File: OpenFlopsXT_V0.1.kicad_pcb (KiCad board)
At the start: 2 copper layers, 83.9 x 68.6 mm, 77 parts, among them J1 UP, J2 DN, J3 R, J4 G, J5 Conn_01x22_Female, J6 OSHW_LOGO, P1 FLOPPY_CONN, P2 POWER_INPUT, P3 POWER_PASSTHRU, P4 PROG_PORT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

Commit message: Corrected Github URL
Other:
- board text added: "https://github.com/pinnet/OpenFlops"
- board text removed: "https://github.com/pinnet/openflops"
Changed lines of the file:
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@@
     (effects (font (size 0.5 0.5) (thickness 0.125)))
   )
-  (gr_text "https://github.com/pinnet/openflops" (at 124.95 128.005) (layer "F.SilkS")
+  (gr_text "https://github.com/pinnet/OpenFlops" (at 124.95 128.005) (layer "F.SilkS")
     (effects (font (size 0.5 0.5) (thickness 0.125)))
   )

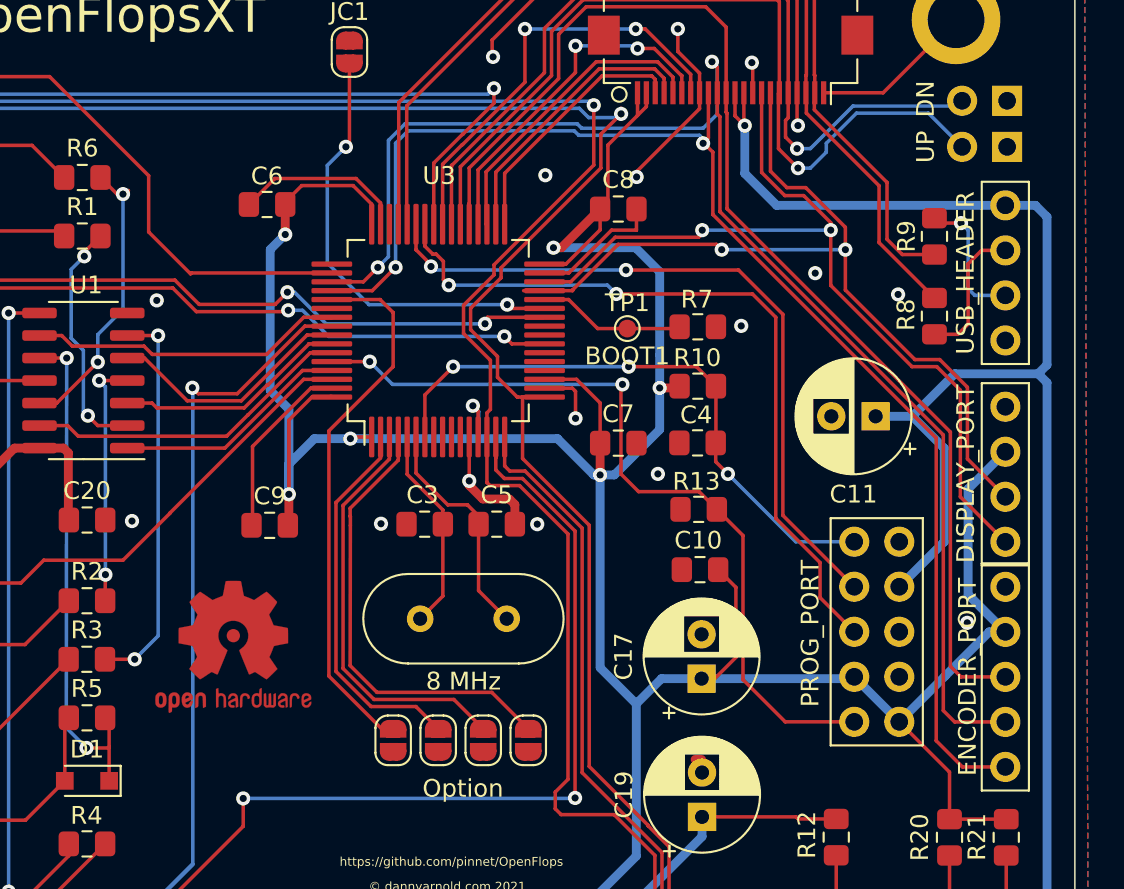
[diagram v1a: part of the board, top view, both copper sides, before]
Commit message: Fixed DRC on OpenFlopsXT
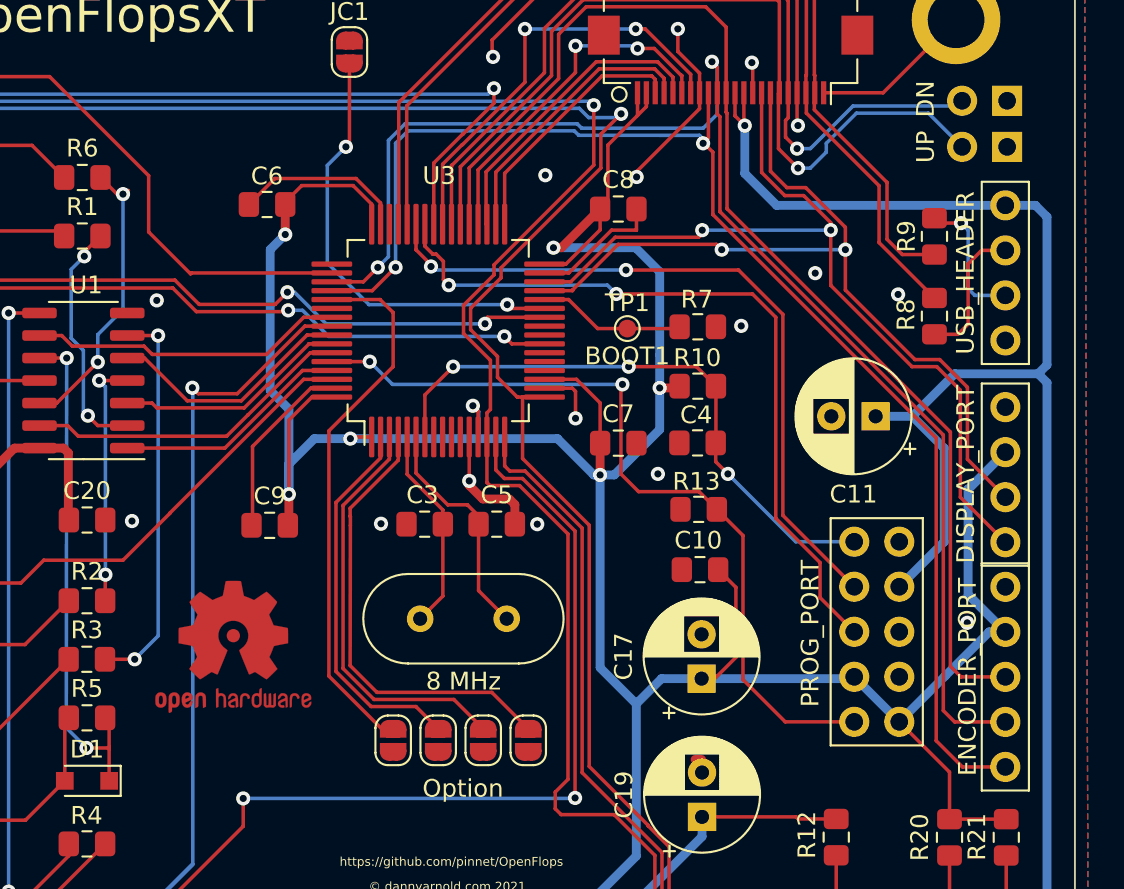
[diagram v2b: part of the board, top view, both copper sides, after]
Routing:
- net /~{step}: track 105.8 -> 104.6 mm
- net /~{enc_sel}: track 69.2 -> 68.0 mm
- net /disp_clk: track 49.1 -> 47.9 mm
- net /nrst: track 34.7 -> 33.9 mm

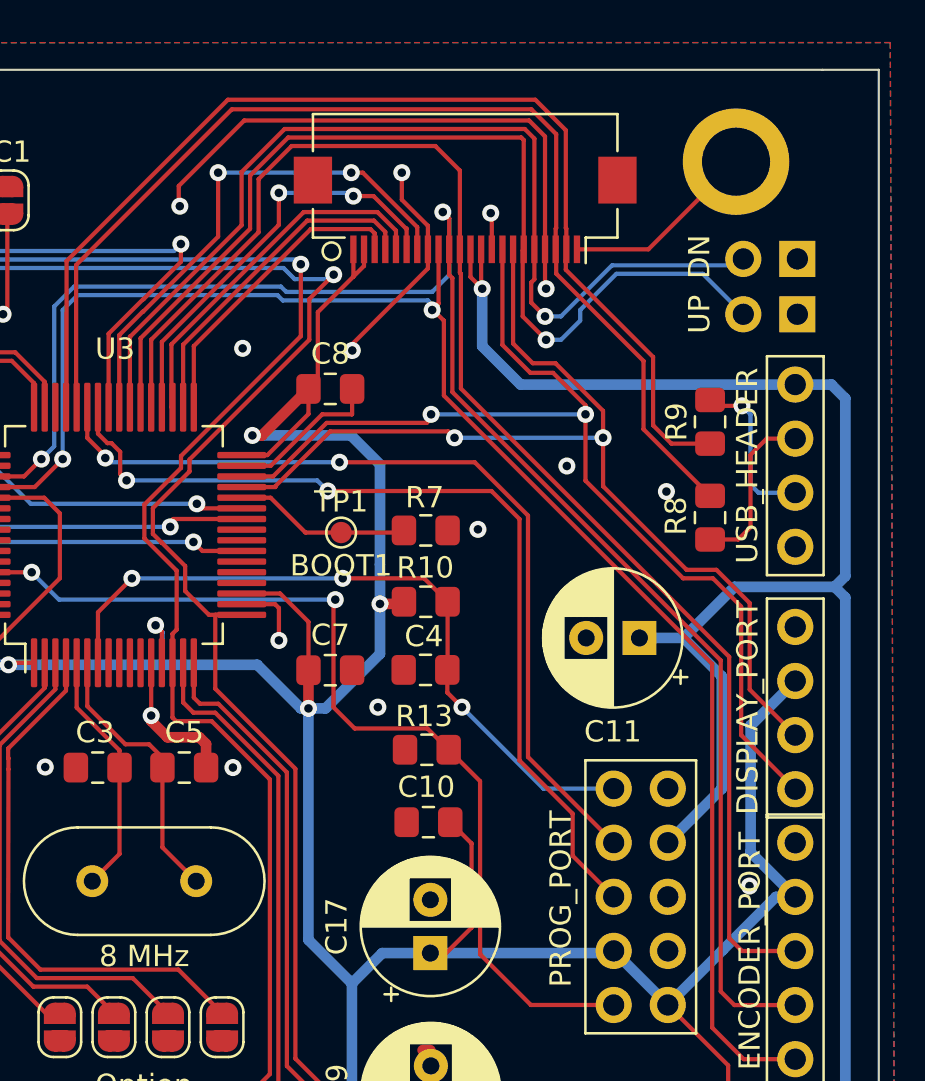
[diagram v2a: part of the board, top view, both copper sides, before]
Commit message: Upgraded Flat Flex Connector OpenFlopsXT
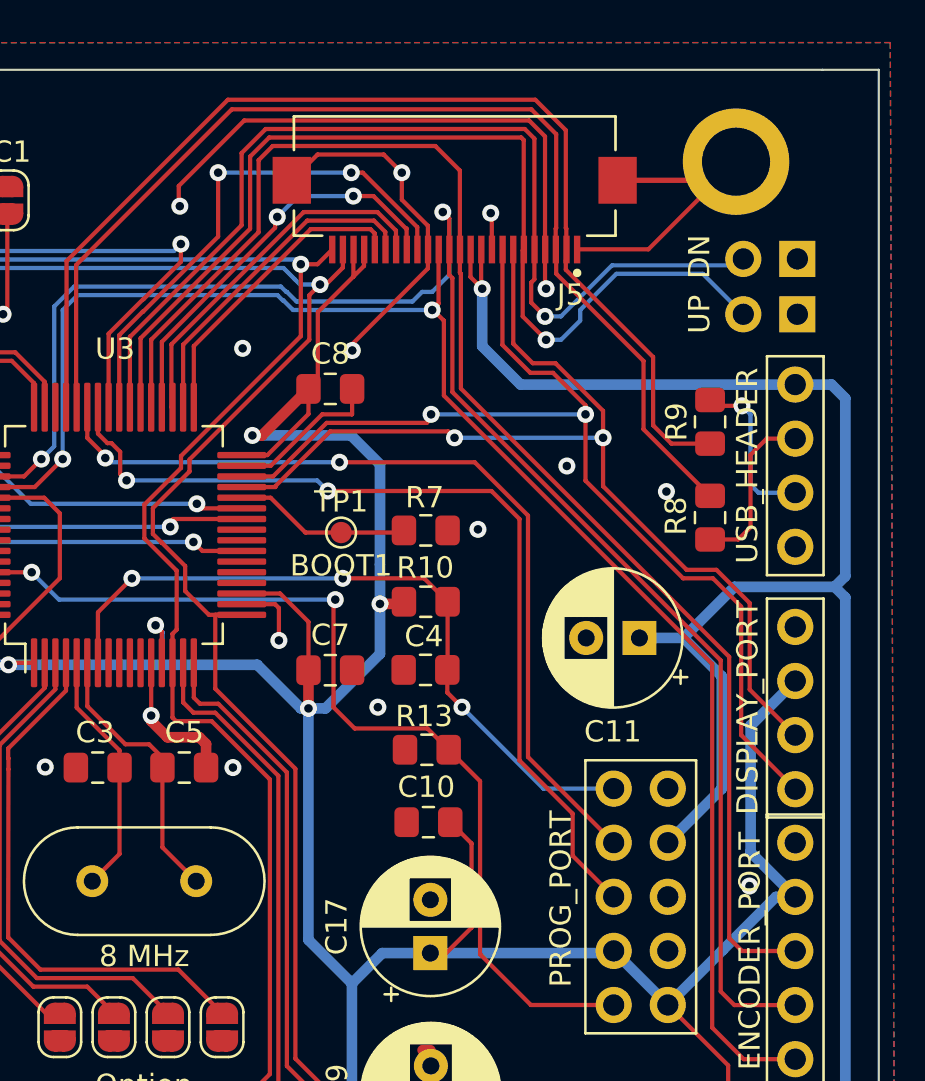
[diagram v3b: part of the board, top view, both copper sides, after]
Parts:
- J5: value Conn_01x22_Female -> FH12-24S-0.5SH(55); footprint CM4IO:Hirose_FH12-22S-0.5SH_1x22-1MP_P0.50mm_Horizontal -> OpenFlops:HRS_FH12-24S-0.5SH(55)
- moved J5 1.06 mm to (140.2, 81.8)
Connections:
- J5 pad 1: +3V3 -> GND
- J5 pad 10: /enc_dt -> +5V
- J5 pad 11: /~{enc_sel} -> +5V
- J5 pad 12: +5V -> /~{enc_sel}
- J5 pad 13: +5V -> /enc_dt
- J5 pad 14: GND -> /enc_clk
- J5 pad 15: /disp_dio -> GND
- J5 pad 16: /disp_clk -> /sd_dtd
- J5 pad 17: /~{key_up} -> /spi_di
- J5 pad 18: /~{key_dn} -> /spi_do
- J5 pad 19: GND -> /spi_clk
- J5 pad 2: +3V3 -> /usb+
- J5 pad 20: /usb- -> /spi_cs
- J5 pad 21: /usb+ -> +3V3
- J5 pad 22: GND -> +3V3
- J5 pad 3: /spi_cs -> /usb-
- J5 pad 4: /spi_clk -> GND
- J5 pad 5: /spi_do -> /~{key_dn}
- J5 pad 6: /spi_di -> /~{key_up}
- J5 pad 7: /sd_dtd -> /disp_clk
- J5 pad 8: GND -> /disp_dio
- J5 pad 9: /enc_clk -> GND
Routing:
- net GND: track 86.2 -> 98.1 mm
- net /~{selx}: track 153.1 -> 154.9 mm
- net /~{sely}: track 142.6 -> 143.5 mm
- net /spi_di: track 20.0 -> 19.3 mm
- net /~{enc_sel}: track 68.0 -> 68.5 mm
- net /~{key_up}: track 48.1 -> 48.7 mm
- net /~{key_dn}: track 47.1 -> 47.6 mm

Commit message: Added 3d images of OpenFlopsXT
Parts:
- moved FID2 35.0 mm to (189.2, 127.0)
- moved C10 35.0 mm to (170.4, 96.2)
- moved C17 35.0 mm to (170.5, 102.4)
- moved C19 35.0 mm to (170.6, 110.2)
- moved H2 35.0 mm to (184.9, 125.4)
- moved J5 35.0 mm to (171.7, 66.6)
- moved JP5 35.0 mm to (153.1, 105.9)
- moved P6 35.0 mm to (187.7, 97.2)
- moved P8 35.0 mm to (187.7, 75.7)
- moved Q7 35.0 mm to (176.9, 122.5)
- moved R10 35.0 mm to (170.3, 85.9)
- moved R11 35.0 mm to (171.8, 123.2)
- moved R7 35.0 mm to (170.3, 82.5)
- moved R8 35.0 mm to (183.7, 81.9)
- moved R9 35.0 mm to (183.7, 77.4)
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
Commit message: Tidy up OpenFlopsXT for manufature
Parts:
- removed P3: POWER_PASSTHRU, OpenFlops:PinHeader_1x04_P2.54mm_Vertical_Power
- moved C1 56.1 mm to (176.6, 85.8), turned to -90 degrees
- moved C19 38.0 mm to (134.9, 123.3)
- moved C10 18.6 mm to (181.2, 111.4), turned to -90 degrees
- moved JC1 12.6 mm to (142.1, 76.3)
- moved C11 11.9 mm to (176.7, 76.3), turned to -90 degrees
- moved C17 1.15 mm to (171.7, 102.2)
- moved FID3 0.29 mm to (144.4, 100.0)
- moved J6 0.29 mm to (144.4, 100.6)
- moved P2 0.13 mm to (111.7, 117.9)
- moved P7 0.12 mm to (187.7, 87.0)
- moved J2 0.09 mm to (187.7, 69.9)
- moved P6 0.07 mm to (187.7, 97.2)
- moved J1 0.06 mm to (187.7, 72.4)
- moved R12 0.05 mm to (178.1, 111.3)
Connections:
- C1 pad 1: +5V -> +3V3
- P6 pad 2: +3V3 -> /~{enc_sel}
- P6 pad 3: /~{enc_sel} -> /enc_dt
- P6 pad 4: /enc_dt -> /enc_clk
- P6 pad 5: /enc_clk -> +3V3
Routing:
- net +5V: track 286.5 -> 262.6 mm, vias 1 -> 2
- net /rx: track 40.7 -> 50.4 mm
- net /~{side}: track 69.0 -> 61.1 mm, vias 1 -> 2
- net /tx: track 42.9 -> 49.8 mm
- net /enc_clk: track 75.7 -> 71.2 mm
- net /spk-: track 8.04 -> 12.1 mm
- net /disp_clk: track 47.9 -> 50.9 mm
- net /jc: track 25.1 -> 22.3 mm
- net unconnected-(P2-Pad4): track 2.79 -> 0.00 mm
- net /~{step}: track 104.6 -> 102.2 mm
- net /~{sely}: track 143.5 -> 145.6 mm, vias 3 -> 4
- net Net-(JP5-Pad2): track 30.6 -> 32.7 mm
- net /~{selx}: track 154.9 -> 153.1 mm, vias 6 -> 7
- net /disp_dio: track 50.0 -> 51.5 mm
- net /usb+r: track 7.74 -> 6.30 mm
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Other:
- board text added: "5V"
- board text added: "GND"
- board text added: "NC"

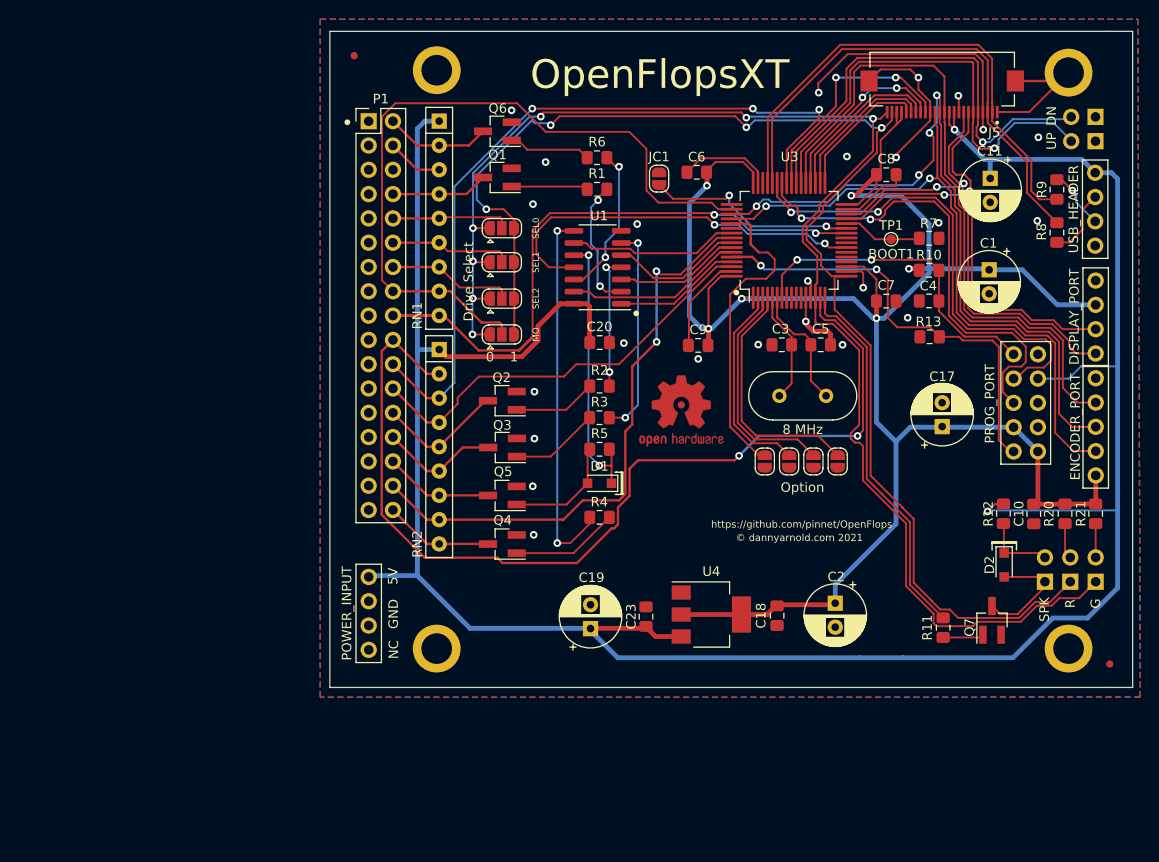
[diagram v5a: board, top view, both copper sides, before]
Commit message: Correct missing pin 1 locators and Tidy up OpenfFLopsXT
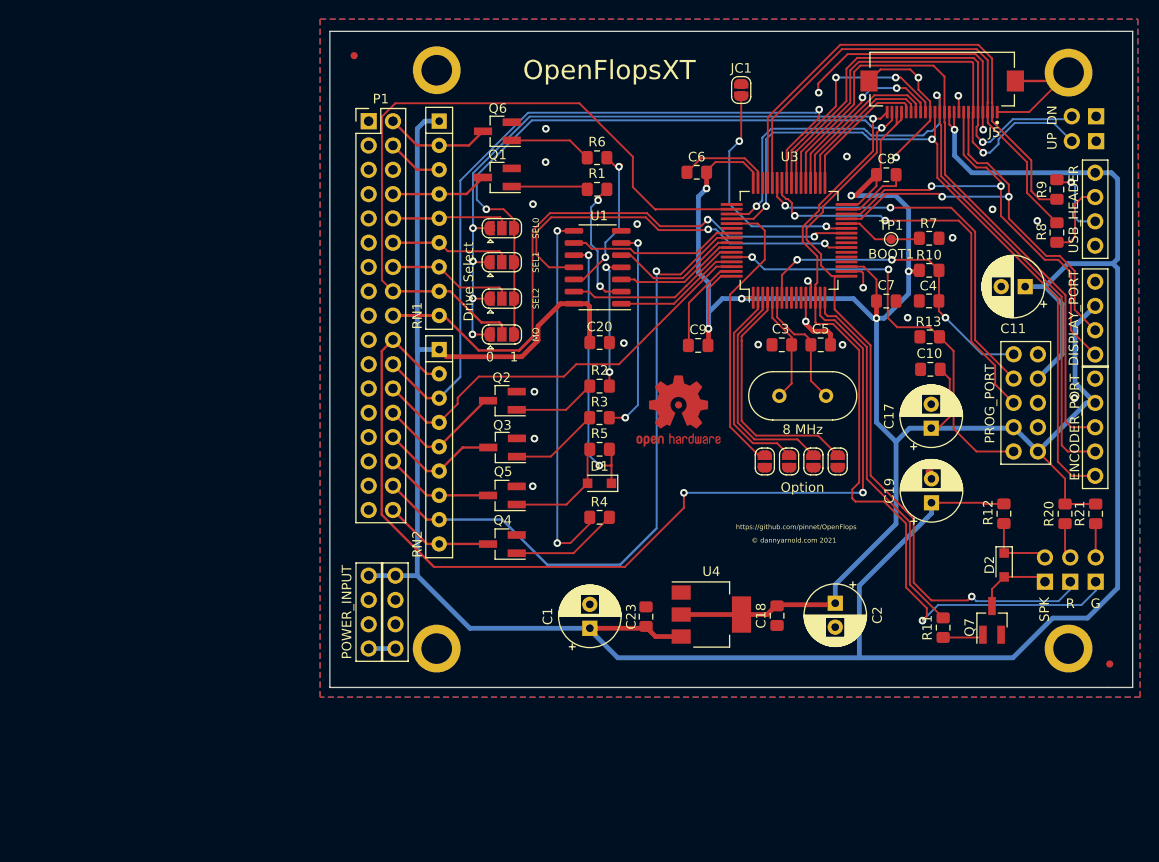
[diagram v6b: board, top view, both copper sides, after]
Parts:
- added P3: POWER_PASSTHRU, OpenFlops:PinHeader_1x04_P2.54mm_Vertical_Power, F.Cu at (114.5, 117.8)
- moved C1 56.1 mm to (134.8, 123.3), turned to 90 degrees
- moved C19 38.0 mm to (170.6, 110.2)
- moved C10 18.6 mm to (170.4, 96.2), turned to 180 degrees
- moved JC1 12.6 mm to (150.7, 67.0)
- moved C11 11.9 mm to (180.3, 87.6), turned to 180 degrees
- moved C17 1.15 mm to (170.5, 102.4)
- moved FID3 0.29 mm to (144.1, 100.0)
- moved J6 0.29 mm to (144.1, 100.6)
- moved P2 0.13 mm to (111.7, 117.8)
- moved P7 0.12 mm to (187.7, 87.1)
- moved J2 0.09 mm to (187.8, 69.8)
- moved P6 0.07 mm to (187.7, 97.2)
- moved J1 0.06 mm to (187.8, 72.4)
- moved R12 0.05 mm to (178.1, 111.3)
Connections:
- C1 pad 1: +3V3 -> +5V
- P6 pad 2: /~{enc_sel} -> +3V3
- P6 pad 3: /enc_dt -> /~{enc_sel}
- P6 pad 4: /enc_clk -> /enc_dt
- P6 pad 5: +3V3 -> /enc_clk
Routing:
- net +5V: track 262.6 -> 286.5 mm, vias 2 -> 1
- net /rx: track 50.4 -> 40.7 mm
- net /~{side}: track 61.1 -> 69.0 mm, vias 2 -> 1
- net /tx: track 49.8 -> 42.9 mm
- net /enc_clk: track 71.2 -> 75.7 mm
- net /spk-: track 12.1 -> 8.04 mm
- net /disp_clk: track 50.9 -> 47.9 mm
- net /jc: track 22.3 -> 25.1 mm
- net unconnected-(P2-Pad4): track 0.00 -> 2.79 mm
- net /~{step}: track 102.2 -> 104.6 mm
- net /~{sely}: track 145.6 -> 143.5 mm, vias 4 -> 3
- net Net-(JP5-Pad2): track 32.7 -> 30.6 mm
- net /~{selx}: track 153.1 -> 154.9 mm, vias 7 -> 6
- net /disp_dio: track 51.5 -> 50.0 mm
- net /usb+r: track 6.30 -> 7.74 mm
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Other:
- board text removed: "5V"
- board text removed: "GND"
- board text removed: "NC"

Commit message: Retreve from backup due to git error
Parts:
- moved C1 56.1 mm to (176.6, 85.8), turned to -90 degrees
- moved C19 38.0 mm to (134.9, 123.3)
- moved C10 18.6 mm to (181.2, 111.4), turned to -90 degrees
- moved JC1 12.6 mm to (142.1, 76.3)
- moved C11 11.9 mm to (176.7, 76.3), turned to -90 degrees
- moved C17 1.15 mm to (171.7, 102.2)
- moved FID3 0.29 mm to (144.4, 100.0)
- moved J6 0.29 mm to (144.4, 100.6)
- moved P7 0.12 mm to (187.7, 87.0)
- moved J2 0.09 mm to (187.7, 69.9)
- moved P6 0.07 mm to (187.7, 97.2)
- moved J1 0.06 mm to (187.7, 72.4)
- moved R12 0.05 mm to (178.1, 111.3)
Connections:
- C1 pad 1: +5V -> +3V3
- P6 pad 2: +3V3 -> /~{enc_sel}
- P6 pad 3: /~{enc_sel} -> /enc_dt
- P6 pad 4: /enc_dt -> /enc_clk
- P6 pad 5: /enc_clk -> +3V3
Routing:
- net +5V: track 286.5 -> 262.6 mm, vias 1 -> 2
- net /rx: track 40.7 -> 50.4 mm
- net /~{side}: track 69.0 -> 61.1 mm, vias 1 -> 2
- net /tx: track 42.9 -> 49.8 mm
- net /enc_clk: track 75.7 -> 71.2 mm
- net /spk-: track 8.04 -> 12.1 mm
- net /disp_clk: track 47.9 -> 50.9 mm
- net /jc: track 25.1 -> 22.3 mm
- net /~{step}: track 104.6 -> 102.2 mm
- net /~{sely}: track 143.5 -> 145.6 mm, vias 3 -> 4
- net Net-(JP5-Pad2): track 30.6 -> 32.7 mm
- net /~{selx}: track 154.9 -> 153.1 mm, vias 6 -> 7
- net /disp_dio: track 50.0 -> 51.5 mm
- net /usb+r: track 7.74 -> 6.30 mm
- net /~{enc_sel}: track 68.5 -> 69.8 mm
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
